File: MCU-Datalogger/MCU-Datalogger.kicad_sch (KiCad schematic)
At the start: 25 parts, among them U1 24LC1025, U2 24LC1025, U3 DS1337S+, U4 ATMEGA328P-AU, Y1 Crystal, Y2 Crystal

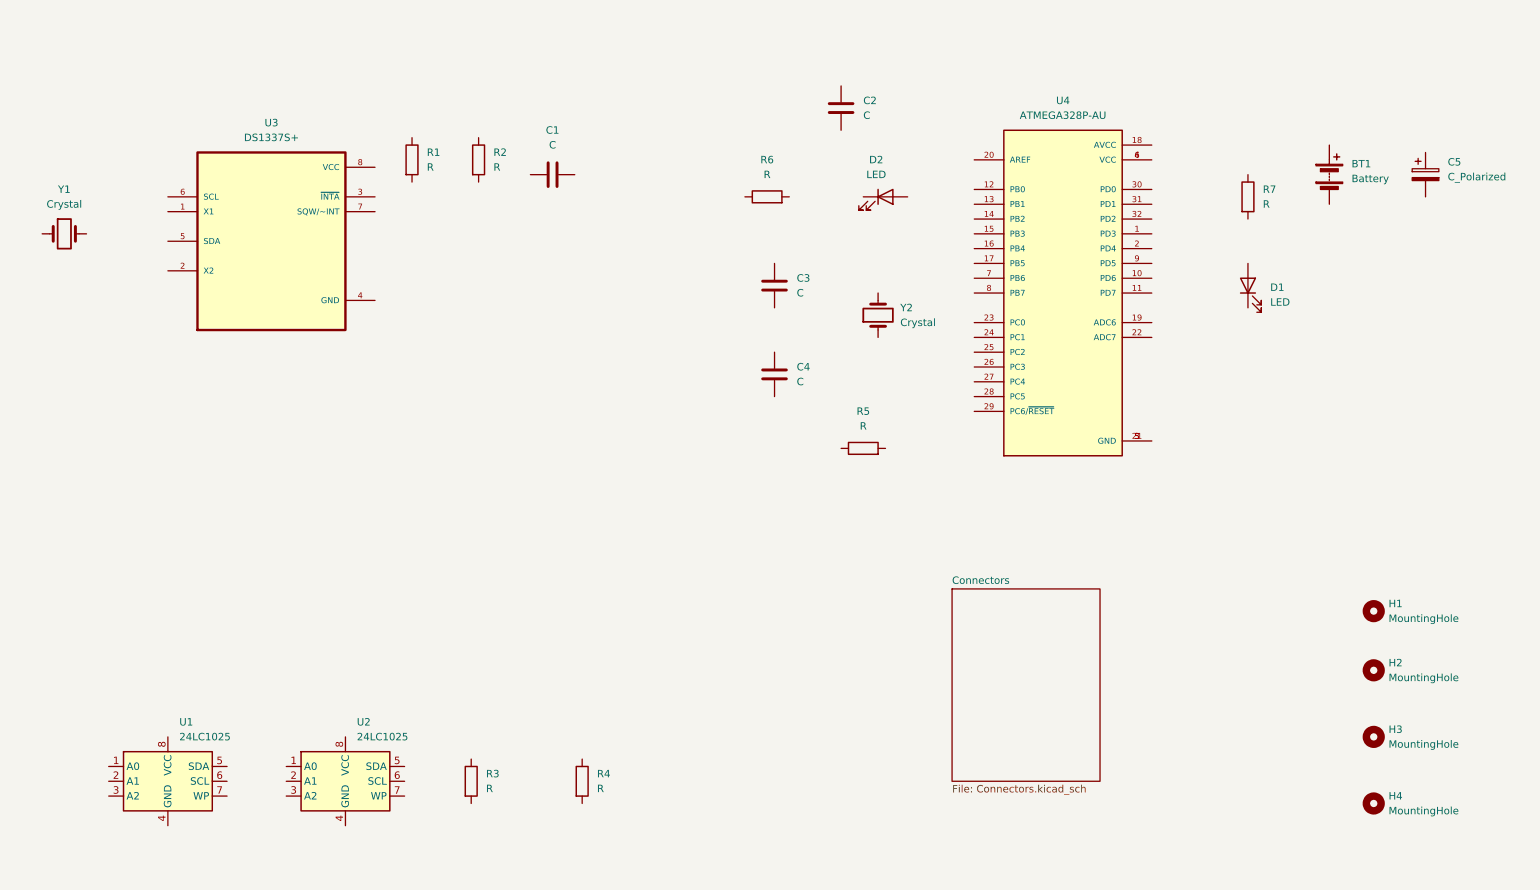
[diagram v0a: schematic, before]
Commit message: Edit component values
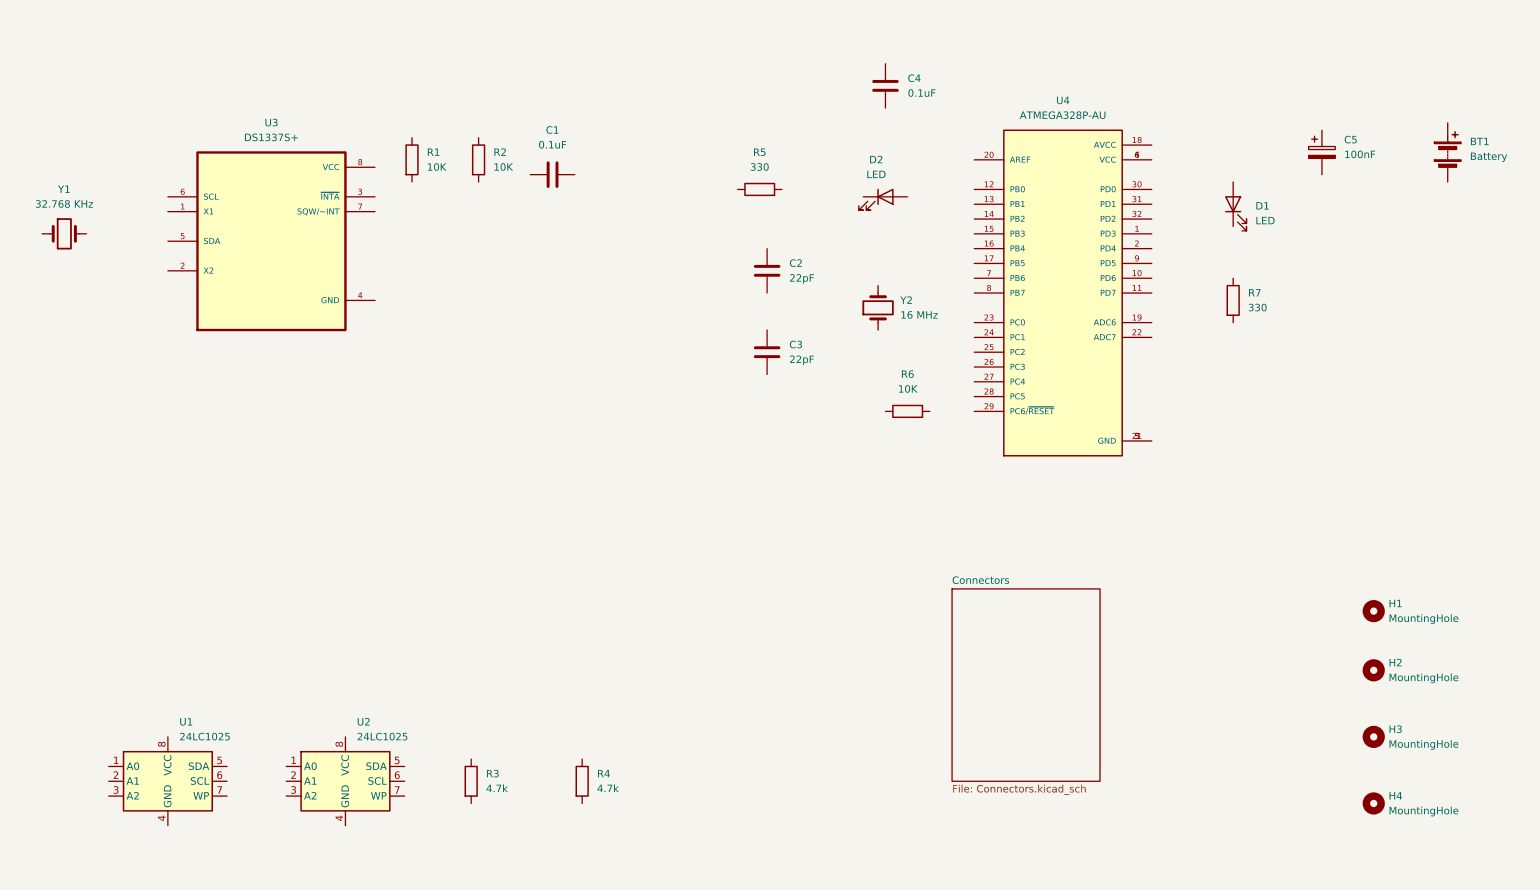
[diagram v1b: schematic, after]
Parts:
- C1, C4: value C -> 0.1uF
- C2, C3: value C -> 22pF
- C5: value C_Polarized -> 100nF
- R1, R2, R6: value R -> 10K
- R3, R4: value R -> 4.7k
- R5, R7: value R -> 330
- Y1: value Crystal -> 32.768 KHz
- Y2: value Crystal -> 16 MHz
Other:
- moved on the sheet: BT1, C2, C3, C4, C5, D1, R5, R6, R7, Y2

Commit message: Associate footprints with symbols
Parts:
- BT1: footprint (none) -> Connector_PinHeader_2.54mm:PinHeader_1x02_P2.54mm_Vertical
- C1, C2, C3, C4, C5: footprint (none) -> Capacitor_SMD:C_0805_2012Metric
- D1, D2: footprint (none) -> LED_SMD:LED_0805_2012Metric
- H1, H2, H3, H4: footprint (none) -> MountingHole:MountingHole_2.1mm
- R1, R2, R3, R4, R5, R6, R7: footprint (none) -> Resistor_SMD:R_0805_2012Metric
- U1, U2: footprint (none) -> Package_SO:SOIC-8_5.23x5.23mm_P1.27mm
- U3: footprint SOIC127P600X175-8N -> Footprints:SOIC127P600X175-8N
- U4: footprint QFP80P900X900X120-32N -> Footprints:QFP80P900X900X120-32N
- Y1, Y2: footprint (none) -> Crystal:Crystal_SMD_5032-2Pin_5.0x3.2mm_HandSoldering
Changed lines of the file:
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@@
       (effects (font (size 1.27 1.27)) (justify left))
     )
-    (property "Footprint" "" (at 257.81 123.19 0)
+    (property "Footprint" "MountingHole:MountingHole_2.1mm" (at 257.81 123.19 0)
       (effects (font (size 1.27 1.27)) hide)
     )
@@
       (effects (font (size 1.27 1.27)))
     )
-    (property "Footprint" "" (at 120.65 47.2948 0)
+    (property "Footprint" "Capacitor_SMD:C_0805_2012Metric" (at 120.65 47.2948 0)
       (effects (font (size 1.27 1.27)) hide)
     )
@@
       (effects (font (size 1.27 1.27)) (justify left))
     )
-    (property "Footprint" "" (at 257.81 133.35 0)
+    (property "Footprint" "MountingHole:MountingHole_2.1mm" (at 257.81 133.35 0)
       (effects (font (size 1.27 1.27)) hide)
     )
@@
       (effects (font (size 1.27 1.27)))
     )
-    (property "Footprint" "QFP80P900X900X120-32N" (at 204.47 68.58 0)
+    (property "Footprint" "Footprints:QFP80P900X900X120-32N" (at 204.47 68.58 0)
       (effects (font (size 1.27 1.27)) (justify bottom) hide)
     )
@@
       (effects (font (size 1.27 1.27)))
     )
-    (property "Footprint" "" (at 173.99 52.07 0)
+    (property "Footprint" "LED_SMD:LED_0805_2012Metric" (at 173.99 52.07 0)
       (effects (font (size 1.27 1.27)) hide)
     )
@@
       (effects (font (size 1.27 1.27)) (justify left))
     )
-    (property "Footprint" "" (at 174.9552 36.83 0)
+    (property "Footprint" "Capacitor_SMD:C_0805_2012Metric" (at 174.9552 36.83 0)
       (effects (font (size 1.27 1.27)) hide)
     )
@@
       (effects (font (size 1.27 1.27)) (justify right))
     )
-    (property "Footprint" "" (at 172.72 71.12 0)
+    (property "Footprint" "Crystal:Crystal_SMD_5032-2Pin_5.0x3.2mm_HandSoldering" (at 172.72 71.12 0)
       (effects (font (size 1.27 1.27)) hide)
     )
@@
       (effects (font (size 1.27 1.27)) (justify left))
     )
-    (property "Footprint" "" (at 249.8852 48.26 0)
+    (property "Footprint" "Capacitor_SMD:C_0805_2012Metric" (at 249.8852 48.26 0)
       (effects (font (size 1.27 1.27)) hide)
     )
@@
       (effects (font (size 1.27 1.27)))
     )
-    (property "Footprint" "" (at 33.02 58.42 0)
+    (property "Footprint" "Crystal:Crystal_SMD_5032-2Pin_5.0x3.2mm_HandSoldering" (at 33.02 58.42 0)
       (effects (font (size 1.27 1.27)) hide)
     )
@@
       (effects (font (size 1.27 1.27)) (justify left))
     )
-    (property "Footprint" "" (at 102.362 45.72 90)
+    (property "Footprint" "Resistor_SMD:R_0805_2012Metric" (at 102.362 45.72 90)
       (effects (font (size 1.27 1.27)) hide)
     )
@@
       (effects (font (size 1.27 1.27)) (justify left))
     )
-    (property "Footprint" "" (at 90.932 45.72 90)
+    (property "Footprint" "Resistor_SMD:R_0805_2012Metric" (at 90.932 45.72 90)
       (effects (font (size 1.27 1.27)) hide)
     )
@@
       (effects (font (size 1.27 1.27)) (justify left))
     )
-    (property "Footprint" "" (at 154.6352 82.55 0)
+    (property "Footprint" "Capacitor_SMD:C_0805_2012Metric" (at 154.6352 82.55 0)
       (effects (font (size 1.27 1.27)) hide)
     )
@@
       (effects (font (size 1.27 1.27)) (justify left))
     )
-    (property "Footprint" "" (at 81.28 152.4 0)
+    (property "Footprint" "Package_SO:SOIC-8_5.23x5.23mm_P1.27mm" (at 81.28 152.4 0)
       (effects (font (size 1.27 1.27)) hide)
     )
@@
       (effects (font (size 1.27 1.27)))
     )
-    (property "Footprint" "SOIC127P600X175-8N" (at 68.58 59.69 0)
+    (property "Footprint" "Footprints:SOIC127P600X175-8N" (at 68.58 59.69 0)
       (effects (font (size 1.27 1.27)) (justify bottom) hide)
     )
     (property "Datasheet" "" (at 68.58 59.69 0)
       (effects (font (size 1.27 1.27)) hide)
+    )
+    (property "Purpose" "" (at 68.58 59.69 0)
+      (effects (font (size 1.27 1.27)))
     )
     (pin "1")
@@
       (effects (font (size 1.27 1.27)) (justify right))
     )
-    (property "Footprint" "" (at 233.68 53.34 0)
+    (property "Footprint" "LED_SMD:LED_0805_2012Metric" (at 233.68 53.34 0)
       (effects (font (size 1.27 1.27)) hide)
     )
@@
       (effects (font (size 1.27 1.27)))
     )
-    (property "Footprint" "" (at 177.8 90.678 90)
+    (property "Footprint" "Resistor_SMD:R_0805_2012Metric" (at 177.8 90.678 90)
       (effects (font (size 1.27 1.27)) hide)
     )
@@
       (effects (font (size 1.27 1.27)) (justify left))
     )
-    (property "Footprint" "" (at 231.902 69.85 90)
+    (property "Footprint" "Resistor_SMD:R_0805_2012Metric" (at 231.902 69.85 90)
       (effects (font (size 1.27 1.27)) hide)
     )
@@
       (effects (font (size 1.27 1.27)))
     )
-    (property "Footprint" "" (at 152.4 52.578 90)
+    (property "Footprint" "Resistor_SMD:R_0805_2012Metric" (at 152.4 52.578 90)
       (effects (font (size 1.27 1.27)) hide)
     )
@@
       (effects (font (size 1.27 1.27)) (justify left))
     )
-    (property "Footprint" "" (at 257.81 144.78 0)
+    (property "Footprint" "MountingHole:MountingHole_2.1mm" (at 257.81 144.78 0)
       (effects (font (size 1.27 1.27)) hide)
     )
@@
       (effects (font (size 1.27 1.27)) (justify left))
     )
-    (property "Footprint" "" (at 50.8 152.4 0)
+    (property "Footprint" "Package_SO:SOIC-8_5.23x5.23mm_P1.27mm" (at 50.8 152.4 0)
       (effects (font (size 1.27 1.27)) hide)
     )
@@
       (effects (font (size 1.27 1.27)) (justify left))
     )
-    (property "Footprint" "" (at 257.81 156.21 0)
+    (property "Footprint" "MountingHole:MountingHole_2.1mm" (at 257.81 156.21 0)
       (effects (font (size 1.27 1.27)) hide)
     )
@@
       (effects (font (size 1.27 1.27)) (justify left))
     )
-    (property "Footprint" "" (at 120.142 152.4 90)
+    (property "Footprint" "Resistor_SMD:R_0805_2012Metric" (at 120.142 152.4 90)
       (effects (font (size 1.27 1.27)) hide)
     )
@@
       (effects (font (size 1.27 1.27)) (justify left))
     )
-    (property "Footprint" "" (at 154.6352 68.58 0)
+    (property "Footprint" "Capacitor_SMD:C_0805_2012Metric" (at 154.6352 68.58 0)
       (effects (font (size 1.27 1.27)) hide)
     )
@@
       (effects (font (size 1.27 1.27)) (justify left))
     )
-    (property "Footprint" "" (at 270.51 42.926 90)
+    (property "Footprint" "Connector_PinHeader_2.54mm:PinHeader_1x02_P2.54mm_Vertical" (at 270.51 42.926 90)
       (effects (font (size 1.27 1.27)) hide)
     )
@@
       (effects (font (size 1.27 1.27)) (justify left))
     )
-    (property "Footprint" "" (at 101.092 152.4 90)
-      (effects (font (size 1.27 1.27)) hide)
-    )
+    (property "Footprint" "Resistor_SMD:R_0805_2012Metric" (at 101.092 152.4 90)
+      (effects (font (size 1.27 1.27)) hide)
+    )

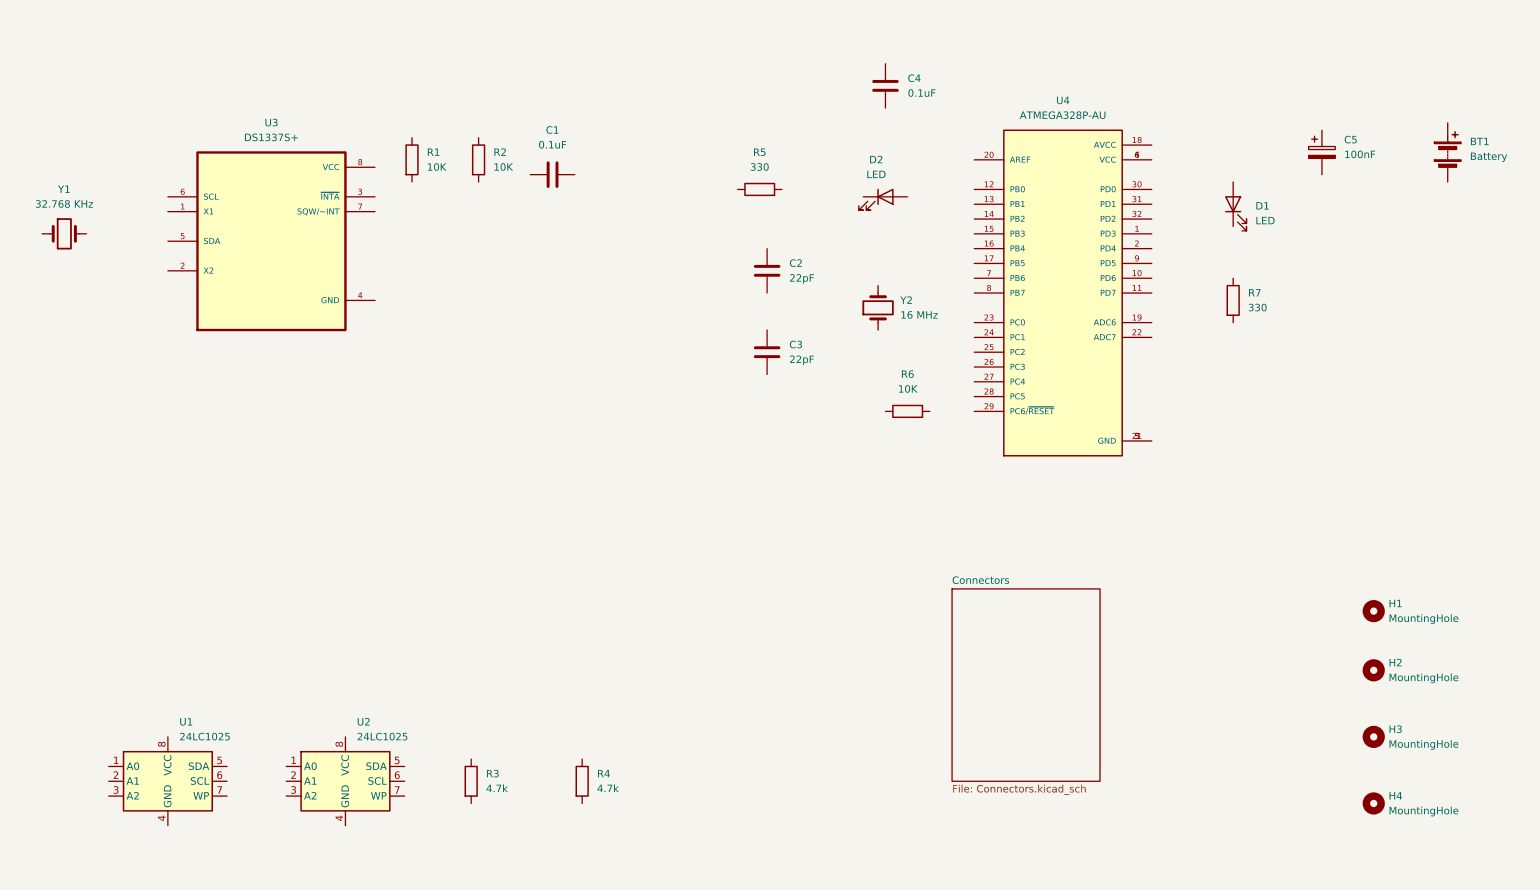
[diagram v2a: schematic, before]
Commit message: Wriring on scheet1
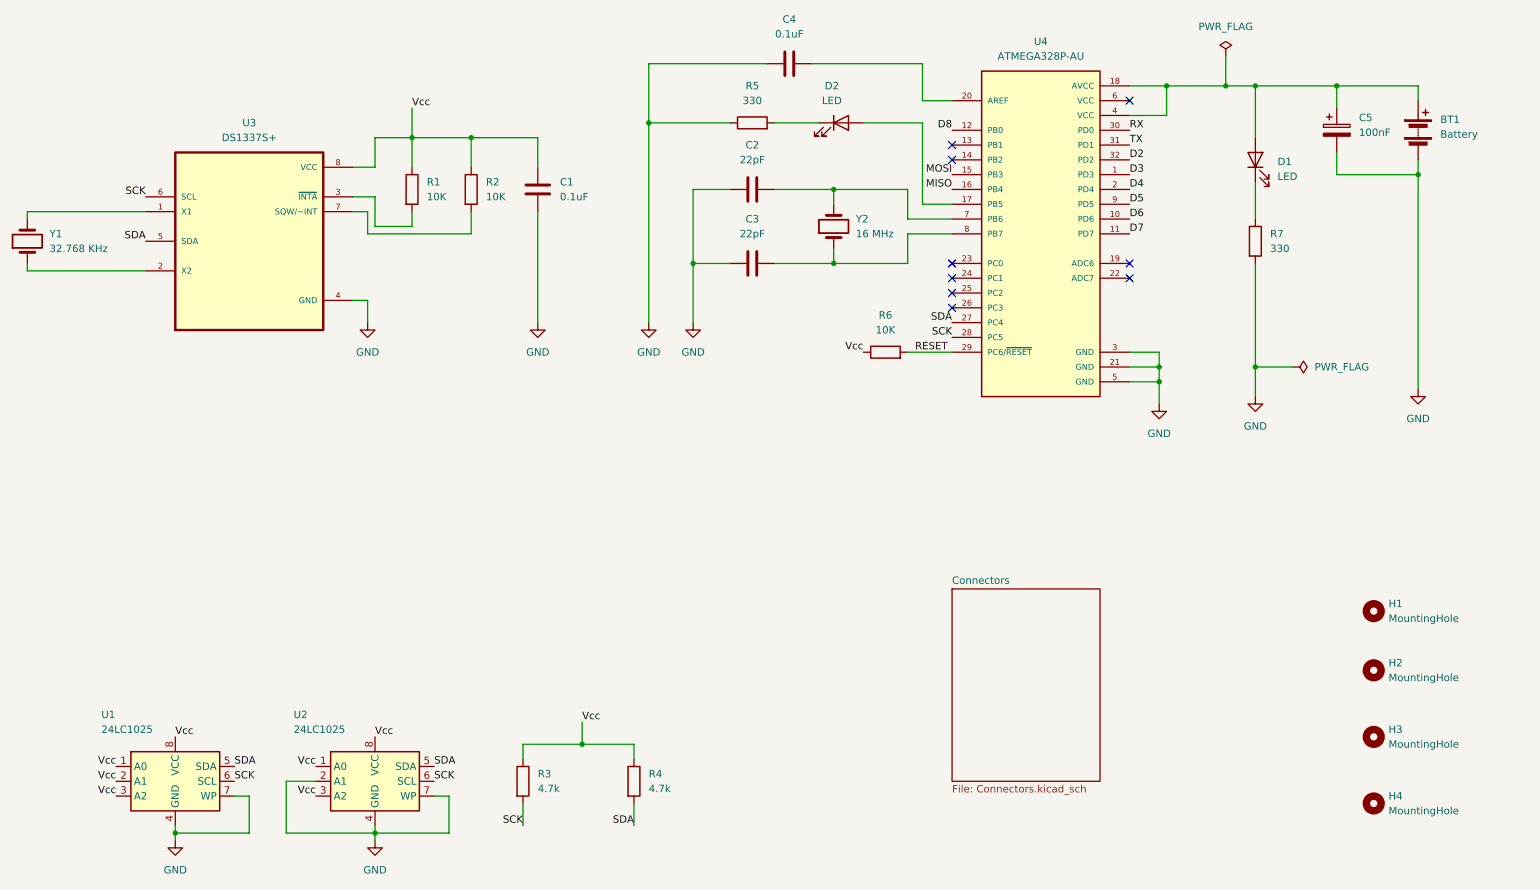
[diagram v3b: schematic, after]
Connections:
- net GND: now reaches C1.1
- net GND: now also BT1.2 (-), C2.1, C3.1, C4.1, C5.2, R5.1, R7.2, U1.4 (GND), U1.7 (WP), U2.2 (A1), U2.4 (GND), U2.7 (WP), U3.4 (GND), U4.21 (GND), U4.3 (GND), U4.5 (GND)
- net Vcc: now reaches C1.2
- net Vcc: now also R1.1, R2.1, R3.1, R4.1, R6.1, U1.1 (A0), U1.2 (A1), U1.3 (A2), U1.8 (VCC), U2.1 (A0), U2.3 (A2), U2.8 (VCC), U3.8 (VCC)
- net D3: now reaches U4.1 (PD3)
- net D6: now reaches U4.10 (PD6)
- net D7: now reaches U4.11 (PD7)
- net D8: now reaches U4.12 (PB0)
- net MOSI: now reaches U4.15 (PB3)
- net MISO: now reaches U4.16 (PB4)
- net at U4.17 (PB5): now also D2.2 (A)
- net at U4.18 (AVCC): now also BT1.1 (+), C5.1, D1.2 (A), U4.4 (VCC)
- net D4: now reaches U4.2 (PD4)
- net at U4.20 (AREF): now also C4.2
- net SDA: now reaches U4.27 (PC4)
- net SDA: now also R4.2, U1.5 (SDA), U2.5 (SDA), U3.5 (SDA)
- net SCK: now reaches U4.28 (PC5)
- net SCK: now also R3.2, U1.6 (SCL), U2.6 (SCL), U3.6 (SCL)
- net RESET: now reaches U4.29 (PC6/~{RESET})
- net RESET: now also R6.2
- net RX: now reaches U4.30 (PD0)
- net TX: now reaches U4.31 (PD1)
- net D2: now reaches U4.32 (PD2)
- net at U4.6 (VCC): no longer U4.4 (VCC)
- net at U4.7 (PB6): now also C2.2, Y2.2
- net at U4.8 (PB7): now also C3.2, Y2.1
- net D5: now reaches U4.9 (PD5)
- net at D2.1 (K): now also R5.2
- net at Y1.1: now also U3.2 (X2)
- net at Y1.2: now also U3.1 (X1)
- net at R2.2: now also U3.7 (SQW/~INT)
- net at R1.2: now also U3.3 (~{INTA})
- net at D1.1 (K): now also R7.1
- no-connect marks 0 -> 9
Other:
- moved on the sheet: BT1, C1, C2, C3, C4, C5, D1, D2, R1, R2, R3, R4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
